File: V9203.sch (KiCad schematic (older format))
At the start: 36 parts, among them J1 RJ45, J4 Screw_Terminal_1x04, U1 V9203, Y1 Crystal_GND24

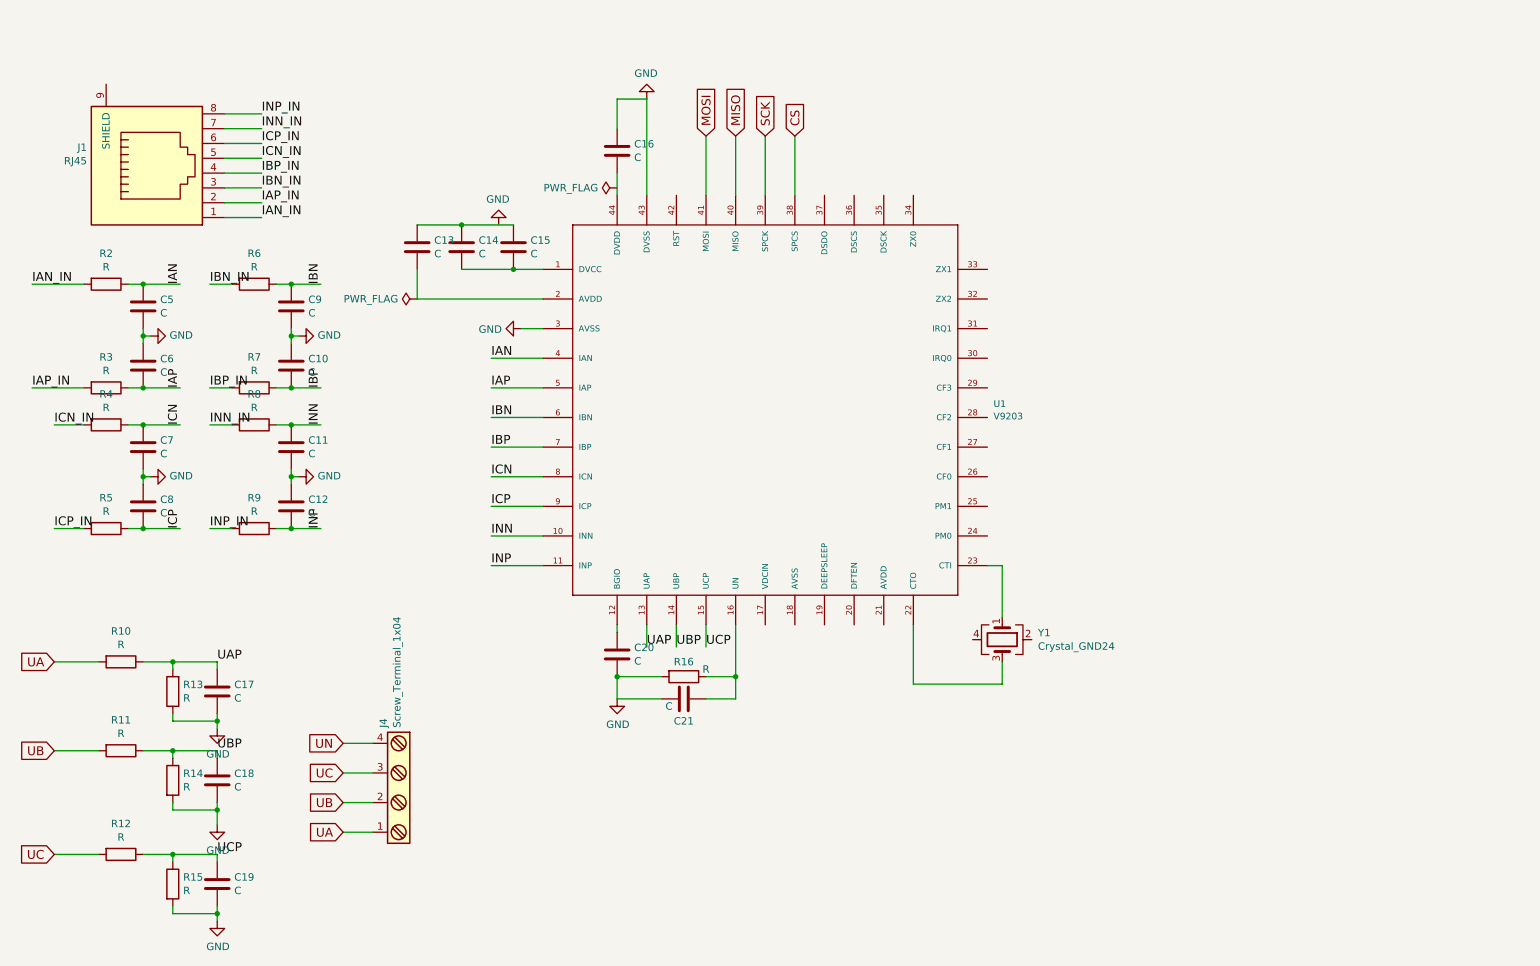
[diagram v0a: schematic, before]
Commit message: Added more parts to featherwing
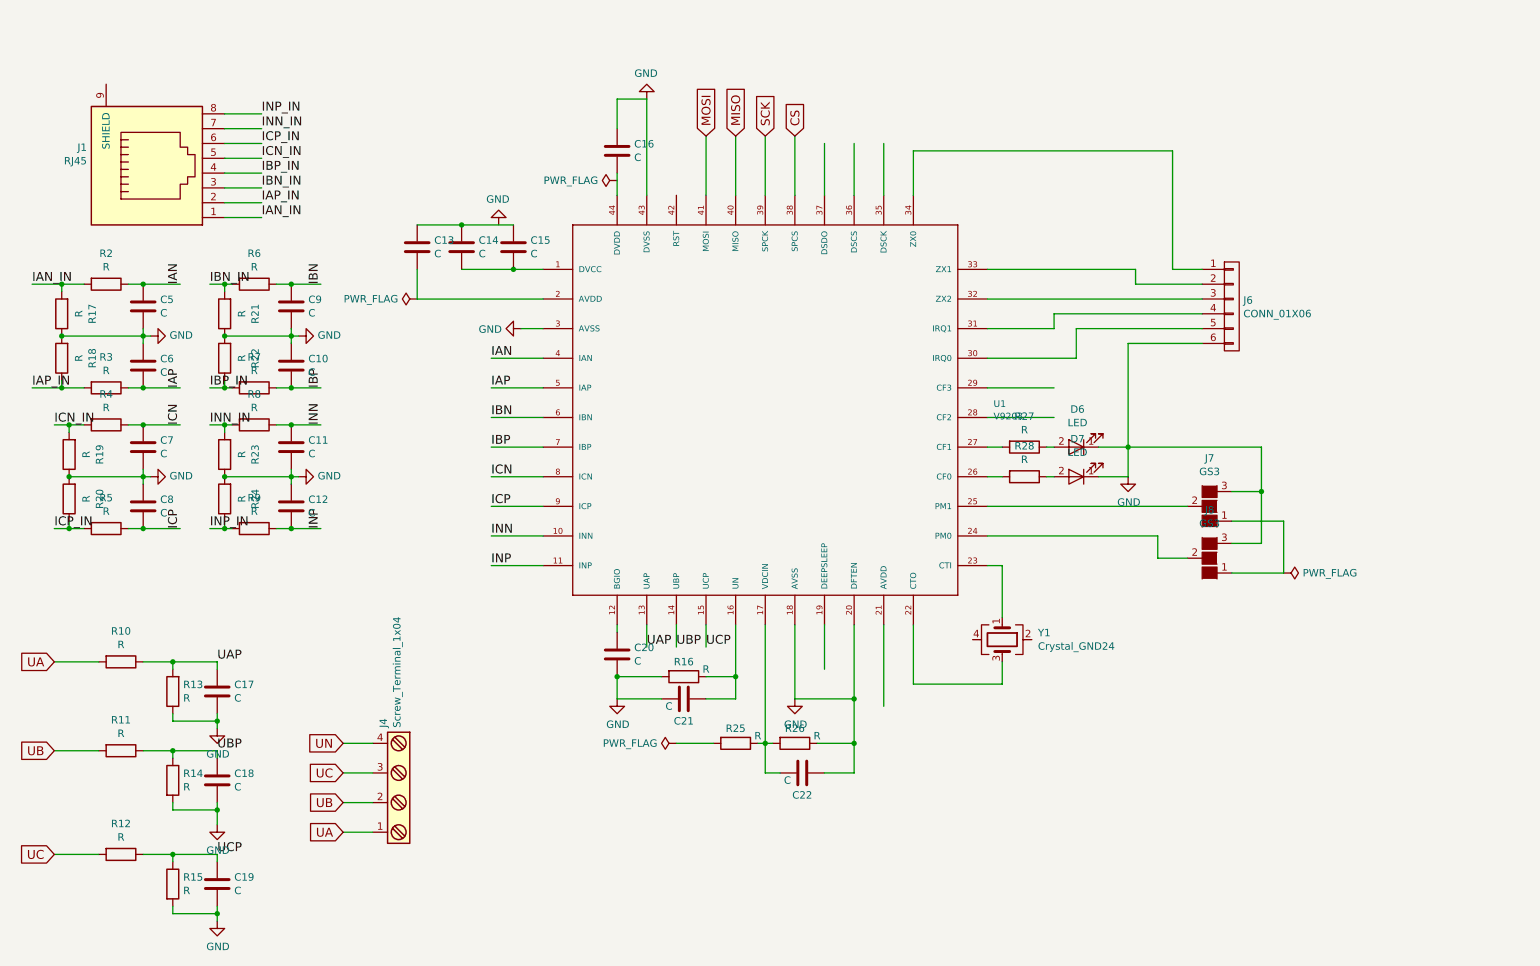
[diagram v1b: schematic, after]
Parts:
- added C22: C, Capacitors_SMD:C_0402, symbol C
- added D6, D7: LED, symbol LED
- added J6: CONN_01X06, symbol CONN_01X06
- added J7, J8: GS3, Connectors:GS3, symbol GS3
- added R17, R18, R19, R20, R21, R22, R23, R24, R25, R26: R, Resistors_SMD:R_0402, symbol R
- added R27, R28: R, symbol R
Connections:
- wire segments 93 -> 149

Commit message: Laid out most parts within PCB bounds
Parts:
- D6, D7: footprint (none) -> LEDs:LED_0603
- J6: footprint (none) -> Connectors_JST:JST_PH_B6B-PH-SM4-TB_06x2.00mm_Straight
- J7, J8: footprint Connectors:GS3 -> Connect:GS3
- R27, R28: footprint (none) -> Resistors_SMD:R_0603_HandSoldering
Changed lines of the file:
@@
 $EndComp
 $Comp
-L GND #PWR11
+L GND #PWR01
 U 1 1 58D7BD25
 P 4900 1350
-F 0 "#PWR11" H 100 -900 50  0001 C CNN
+F 0 "#PWR01" H 100 -900 50  0001 C CNN
 F 1 "GND" H 4905 1177 50  0000 C CNN
 F 2 "" H 100 -650 50  0001 C CNN
@@
 $EndComp
 $Comp
-L PWR_FLAG #FLG2
+L PWR_FLAG #FLG02
 U 1 1 58D7C0C0
 P 4700 1900
-F 0 "#FLG2" H -150 75  50  0001 C CNN
+F 0 "#FLG02" H -150 75  50  0001 C CNN
 F 1 "PWR_FLAG" V 4700 2028 50  0000 L CNN
 F 2 "" H -150 0   50  0001 C CNN
@@
 $EndComp
 $Comp
-L GND #PWR9
+L GND #PWR03
 U 1 1 58D7CCEA
 P 4050 2900
-F 0 "#PWR9" H -750 650 50  0001 C CNN
+F 0 "#PWR03" H -750 650 50  0001 C CNN
 F 1 "GND" V 4055 2772 50  0000 R CNN
 F 2 "" H -750 900 50  0001 C CNN
@@
 $EndComp
 $Comp
-L GND #PWR8
+L GND #PWR04
 U 1 1 58D7CDA6
 P 3900 2200
-F 0 "#PWR8" H -900 -50 50  0001 C CNN
+F 0 "#PWR04" H -900 -50 50  0001 C CNN
 F 1 "GND" H 3905 2027 50  0000 C CNN
 F 2 "" H -900 200 50  0001 C CNN
@@
 $EndComp
 $Comp
-L PWR_FLAG #FLG1
+L PWR_FLAG #FLG05
 U 1 1 58D7CE59
 P 3350 2700
-F 0 "#FLG1" H -1500 875 50  0001 C CNN
+F 0 "#FLG05" H -1500 875 50  0001 C CNN
 F 1 "PWR_FLAG" V 3350 2828 50  0000 L CNN
 F 2 "" H -1500 800 50  0001 C CNN
@@
 $EndComp
 $Comp
-L GND #PWR1
+L GND #PWR06
 U 1 1 58D7E932
 P 1550 2950
-F 0 "#PWR1" H -3250 700 50  0001 C CNN
+F 0 "#PWR06" H -3250 700 50  0001 C CNN
 F 1 "GND" V 1555 2822 50  0000 R CNN
 F 2 "" H -3250 950 50  0001 C CNN
@@
 $EndComp
 $Comp
-L GND #PWR2
+L GND #PWR07
 U 1 1 58D7EE20
 P 1550 3900
-F 0 "#PWR2" H -3250 1650 50  0001 C CNN
+F 0 "#PWR07" H -3250 1650 50  0001 C CNN
 F 1 "GND" V 1555 3772 50  0000 R CNN
 F 2 "" H -3250 1900 50  0001 C CNN
@@
 $EndComp
 $Comp
-L GND #PWR7
+L GND #PWR08
 U 1 1 58D7EE5B
 P 2550 3900
-F 0 "#PWR7" H -2250 1650 50  0001 C CNN
+F 0 "#PWR08" H -2250 1650 50  0001 C CNN
 F 1 "GND" V 2555 3772 50  0000 R CNN
 F 2 "" H -2250 1900 50  0001 C CNN
@@
 $EndComp
 $Comp
-L GND #PWR6
+L GND #PWR09
 U 1 1 58D7EE96
 P 2550 2950
-F 0 "#PWR6" H -2250 700 50  0001 C CNN
+F 0 "#PWR09" H -2250 700 50  0001 C CNN
 F 1 "GND" V 2555 2822 50  0000 R CNN
 F 2 "" H -2250 950 50  0001 C CNN
@@
 $EndComp
 $Comp
-L GND #PWR3
+L GND #PWR010
 U 1 1 58D8C933
 P 2000 5600
-F 0 "#PWR3" H -2800 3350 50  0001 C CNN
+F 0 "#PWR010" H -2800 3350 50  0001 C CNN
 F 1 "GND" H 2005 5427 50  0000 C CNN
 F 2 "" H -2800 3600 50  0001 C CNN
@@
 $EndComp
 $Comp
-L GND #PWR4
+L GND #PWR011
 U 1 1 58D8CC7A
 P 2000 6250
-F 0 "#PWR4" H -2800 4000 50  0001 C CNN
+F 0 "#PWR011" H -2800 4000 50  0001 C CNN
 F 1 "GND" H 2005 6077 50  0000 C CNN
 F 2 "" H -2800 4250 50  0001 C CNN
@@
 $EndComp
 $Comp
-L GND #PWR5
+L GND #PWR012
 U 1 1 58D8CE39
 P 2000 6900
-F 0 "#PWR5" H -2800 4650 50  0001 C CNN
+F 0 "#PWR012" H -2800 4650 50  0001 C CNN
 F 1 "GND" H 2005 6727 50  0000 C CNN
 F 2 "" H -2800 4900 50  0001 C CNN
@@
 $EndComp
 $Comp
-L GND #PWR10
+L GND #PWR013
 U 1 1 58D8D54A
 P 4700 5400
-F 0 "#PWR10" H -100 3150 50  0001 C CNN
+F 0 "#PWR013" H -100 3150 50  0001 C CNN
 F 1 "GND" H 4705 5227 50  0000 C CNN
 F 2 "" H -100 3400 50  0001 C CNN
@@
 F 0 "D7" H 7792 3645 50  0000 C CNN
 F 1 "LED" H 7792 3736 50  0000 C CNN
-F 2 "" H -550 250 50  0001 C CNN
+F 2 "LEDs:LED_0603" H -550 250 50  0001 C CNN
 F 3 "" H -550 250 50  0001 C CNN
 	1    7800 3900
@@
 F 0 "D6" H 7792 3445 50  0000 C CNN
 F 1 "LED" H 7792 3536 50  0000 C CNN
-F 2 "" H -550 50  50  0001 C CNN
+F 2 "LEDs:LED_0603" H -550 50  50  0001 C CNN
 F 3 "" H -550 50  50  0001 C CNN
 	1    7800 3700
@@
 F 0 "R27" V 7243 3700 50  0000 C CNN
 F 1 "R" V 7334 3700 50  0000 C CNN
-F 2 "" V -70 0   50  0001 C CNN
+F 2 "Resistors_SMD:R_0603_HandSoldering" V -70 0   50  0001 C CNN
 F 3 "" H 0   0   50  0001 C CNN
 	1    7450 3700
@@
 F 0 "R28" V 7243 3900 50  0000 C CNN
 F 1 "R" V 7334 3900 50  0000 C CNN
-F 2 "" V -70 200 50  0001 C CNN
+F 2 "Resistors_SMD:R_0603_HandSoldering" V -70 200 50  0001 C CNN
 F 3 "" H 0   200 50  0001 C CNN
 	1    7450 3900
@@
 $EndComp
 $Comp
-L GND #PWR13
+L GND #PWR014
 U 1 1 58EFA437
 P 8150 3900
-F 0 "#PWR13" H 3350 1650 50  0001 C CNN
+F 0 "#PWR014" H 3350 1650 50  0001 C CNN
 F 1 "GND" H 8155 3727 50  0000 C CNN
 F 2 "" H 3350 1900 50  0001 C CNN
@@
 $EndComp
 $Comp
-L GND #PWR12
+L GND #PWR015
 U 1 1 58EFBDC4
 P 5900 5400
-F 0 "#PWR12" H 1100 3150 50  0001 C CNN
+F 0 "#PWR015" H 1100 3150 50  0001 C CNN
 F 1 "GND" H 5905 5227 50  0000 C CNN
 F 2 "" H 1100 3400 50  0001 C CNN
@@
 $EndComp
 $Comp
-L PWR_FLAG #FLG3
+L PWR_FLAG #FLG016
 U 1 1 58EFD209
 P 5100 5700
-F 0 "#FLG3" H 250 3875 50  0001 C CNN
+F 0 "#FLG016" H 250 3875 50  0001 C CNN
 F 1 "PWR_FLAG" V 5100 5828 50  0000 L CNN
 F 2 "" H 250 3800 50  0001 C CNN
@@
 F 0 "J6" H 8928 2791 50  0000 L CNN
 F 1 "CONN_01X06" H 8928 2700 50  0000 L CNN
-F 2 "" H -100 150 50  0001 C CNN
+F 2 "Connectors_JST:JST_PH_B6B-PH-SM4-TB_06x2.00mm_Straight" H -100 150 50  0001 C CNN
 F 3 "" H -100 150 50  0001 C CNN
 	1    8850 2750
@@
 F 0 "J7" H 8700 3775 50  0000 C CNN
 F 1 "GS3" H 8700 3866 50  0000 C CNN
-F 2 "Connectors:GS3" V -762 -1174 50  0001 C CNN
+F 2 "Connect:GS3" V -762 -1174 50  0001 C CNN
 F 3 "" H -850 -1100 50  0001 C CNN
 	1    8700 4100
@@
 F 0 "J8" H 8700 4125 50  0000 C CNN
 F 1 "GS3" H 8700 4216 50  0000 C CNN
-F 2 "Connectors:GS3" V -762 -824 50  0001 C CNN
+F 2 "Connect:GS3" V -762 -824 50  0001 C CNN
 F 3 "" H -850 -750 50  0001 C CNN
 	1    8700 4450
@@
 Connection ~ 9050 4000
 $Comp
-L PWR_FLAG #FLG4
+L PWR_FLAG #FLG017
 U 1 1 58F50052
 P 9200 4550
-F 0 "#FLG4" H 4350 2725 50  0001 C CNN
+F 0 "#FLG017" H 4350 2725 50  0001 C CNN
 F 1 "PWR_FLAG" V 9200 4678 50  0000 L CNN
 F 2 "" H 4350 2650 50  0001 C CNN

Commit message: Neaten up parts layout
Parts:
- added C? (x4): C, Capacitors_SMD:C_0402, symbol C
- added R? (x4): R, Resistors_SMD:R_0402, symbol R
- R17, R18, R19, R20, R21, R22, R23, R24: footprint Resistors_SMD:R_0402 -> Resistors_SMD:R_0603
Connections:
- net labels added: +3V3, V_CLK, V_CS, V_MISO, V_MOSI
- wire segments 149 -> 167
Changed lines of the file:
@@
 Text Label 3850 4500 0    60   ~ 0
 INP
-Text GLabel 5300 1600 1    60   Input ~ 0
-MOSI
-Text GLabel 5500 1600 1    60   Input ~ 0
-MISO
-Text GLabel 5700 1600 1    60   Input ~ 0
-SCK
-Text GLabel 5900 1600 1    60   Input ~ 0
-CS
 $Comp
 L LED D7
@@
 F 0 "R17" V 743 2800 50  0000 C CNN
 F 1 "R" V 834 2800 50  0000 C CNN
-F 2 "Resistors_SMD:R_0402" V -1670 650 50  0001 C CNN
+F 2 "Resistors_SMD:R_0603" V -1670 650 50  0001 C CNN
 F 3 "" H -1600 650 50  0001 C CNN
 	1    950  2800
@@
 F 0 "R18" V 743 3100 50  0000 C CNN
 F 1 "R" V 834 3100 50  0000 C CNN
-F 2 "Resistors_SMD:R_0402" V -1670 950 50  0001 C CNN
+F 2 "Resistors_SMD:R_0603" V -1670 950 50  0001 C CNN
 F 3 "" H -1600 950 50  0001 C CNN
 	1    950  3100
@@
 F 0 "R21" V 1843 2800 50  0000 C CNN
 F 1 "R" V 1934 2800 50  0000 C CNN
-F 2 "Resistors_SMD:R_0402" V -570 650 50  0001 C CNN
+F 2 "Resistors_SMD:R_0603" V -570 650 50  0001 C CNN
 F 3 "" H -500 650 50  0001 C CNN
 	1    2050 2800
@@
 F 0 "R22" V 1843 3100 50  0000 C CNN
 F 1 "R" V 1934 3100 50  0000 C CNN
-F 2 "Resistors_SMD:R_0402" V -570 950 50  0001 C CNN
+F 2 "Resistors_SMD:R_0603" V -570 950 50  0001 C CNN
 F 3 "" H -500 950 50  0001 C CNN
 	1    2050 3100
@@
 F 0 "R19" V 793 3750 50  0000 C CNN
 F 1 "R" V 884 3750 50  0000 C CNN
-F 2 "Resistors_SMD:R_0402" V -1620 1600 50  0001 C CNN
+F 2 "Resistors_SMD:R_0603" V -1620 1600 50  0001 C CNN
 F 3 "" H -1550 1600 50  0001 C CNN
 	1    1000 3750
@@
 F 0 "R20" V 793 4050 50  0000 C CNN
 F 1 "R" V 884 4050 50  0000 C CNN
-F 2 "Resistors_SMD:R_0402" V -1620 1900 50  0001 C CNN
+F 2 "Resistors_SMD:R_0603" V -1620 1900 50  0001 C CNN
 F 3 "" H -1550 1900 50  0001 C CNN
 	1    1000 4050
@@
 F 0 "R23" V 1843 3750 50  0000 C CNN
 F 1 "R" V 1934 3750 50  0000 C CNN
-F 2 "Resistors_SMD:R_0402" V -570 1600 50  0001 C CNN
+F 2 "Resistors_SMD:R_0603" V -570 1600 50  0001 C CNN
 F 3 "" H -500 1600 50  0001 C CNN
 	1    2050 3750
@@
 F 0 "R24" V 1843 4050 50  0000 C CNN
 F 1 "R" V 1934 4050 50  0000 C CNN
-F 2 "Resistors_SMD:R_0402" V -570 1900 50  0001 C CNN
+F 2 "Resistors_SMD:R_0603" V -570 1900 50  0001 C CNN
 F 3 "" H -500 1900 50  0001 C CNN
 	1    2050 4050
@@
 	0    1    1    0
 $EndComp
+Text GLabel 5200 5700 3    60   Input ~ 0
++3V3
+Text GLabel 9100 4550 3    60   Input ~ 0
++3V3
+$Comp
+L R R?
+U 1 1 58FE5B05
+P 10100 2450
+F 0 "R?" V 9893 2450 50  0000 C CNN
+F 1 "R" V 9984 2450 50  0000 C CNN
+F 2 "Resistors_SMD:R_0402" V 7480 300 50  0001 C CNN
+F 3 "" H 7550 300 50  0001 C CNN
+	1    10100 2450
+	0    1    1    0
+$EndComp
+$Comp
+L C C?
+U 1 1 58FE5BE7
+P 10300 2650
+F 0 "C?" H 10415 2696 50  0000 L CNN
+F 1 "C" H 10415 2605 50  0000 L CNN
+F 2 "Capacitors_SMD:C_0402" H 8738 -450 50  0001 C CNN
+F 3 "" H 8700 -300 50  0001 C CNN
+	1    10300 2650
+	1    0    0    -1
+$EndComp
+$Comp
+L R R?
+U 1 1 58FE5CF5
+P 10100 3000
+F 0 "R?" V 9893 3000 50  0000 C CNN
+F 1 "R" V 9984 3000 50  0000 C CNN
+F 2 "Resistors_SMD:R_0402" V 7480 850 50  0001 C CNN
+F 3 "" H 7550 850 50  0001 C CNN
+	1    10100 3000
+	0    1    1    0
+$EndComp
+$Comp
+L C C?
+U 1 1 58FE5D9B
+P 10300 3200
+F 0 "C?" H 10415 3246 50  0000 L CNN
+F 1 "C" H 10415 3155 50  0000 L CNN
+F 2 "Capacitors_SMD:C_0402" H 8738 100 50  0001 C CNN
+F 3 "" H 8700 250 50  0001 C CNN
+	1    10300 3200
+	1    0    0    -1
+$EndComp
+$Comp
+L R R?
+U 1 1 58FE5E43
+P 10050 3500
+F 0 "R?" V 9843 3500 50  0000 C CNN
+F 1 "R" V 9934 3500 50  0000 C CNN
+F 2 "Resistors_SMD:R_0402" V 7430 1350 50  0001 C CNN
+F 3 "" H 7500 1350 50  0001 C CNN
+	1    10050 3500
+	0    1    1    0
+$EndComp
+$Comp
+L C C?
+U 1 1 58FE5EEF
+P 10300 3700
+F 0 "C?" H 10415 3746 50  0000 L CNN
+F 1 "C" H 10415 3655 50  0000 L CNN
+F 2 "Capacitors_SMD:C_0402" H 8738 600 50  0001 C CNN
+F 3 "" H 8700 750 50  0001 C CNN
+	1    10300 3700
+	1    0    0    -1
+$EndComp
+$Comp
+L C C?
+U 1 1 58FE5F95
+P 9850 4250
+F 0 "C?" H 9965 4296 50  0000 L CNN
+F 1 "C" H 9965 4205 50  0000 L CNN
+F 2 "Capacitors_SMD:C_0402" H 8288 1150 50  0001 C CNN
+F 3 "" H 8250 1300 50  0001 C CNN
+	1    9850 4250
+	1    0    0    -1
+$EndComp
+$Comp
+L R R?
+U 1 1 58FE6045
+P 10050 4000
+F 0 "R?" V 9843 4000 50  0000 C CNN
+F 1 "R" V 9934 4000 50  0000 C CNN
+F 2 "Resistors_SMD:R_0402" V 7430 1850 50  0001 C CNN
+F 3 "" H 7500 1850 50  0001 C CNN
+	1    10050 4000
+	0    1    1    0
+$EndComp
+Text Label 5300 1600 1    60   ~ 0
+V_MOSI
+Text Label 5500 1600 1    60   ~ 0
+V_MISO
+Text Label 5700 1600 1    60   ~ 0
+V_CLK
+Text Label 5900 1600 1    60   ~ 0
+V_CS
+Wire Wire Line
+	10250 2450 10450 2450
+Wire Wire Line
+	10300 2450 10300 2500
+Connection ~ 10300 2450
+Wire Wire Line
+	10250 3000 10450 3000
+Wire Wire Line
+	10300 3000 10300 3050
+Connection ~ 10300 3000
+Wire Wire Line
+	10200 3500 10450 3500
+Wire Wire Line
+	10300 3500 10300 3550
+Connection ~ 10300 3500
+Wire Wire Line
+	9850 4100 9850 4000
+Connection ~ 9850 4000
+Wire Wire Line
+	10200 4000 10400 4000
+$Comp
+L GND #PWR?
+U 1 1 58FE85DB
+P 10600 4500
+F 0 "#PWR?" H 5800 2250 50  0001 C CNN
+F 1 "GND" H 10605 4327 50  0000 C CNN
+F 2 "" H 5800 2500 50  0001 C CNN
+F 3 "" H 5800 2500 50  0001 C CNN
+	1    10600 4500
+	1    0    0    -1
+$EndComp
+Wire Wire Line
+	9850 4400 9850 4500
+Wire Wire Line
+	9850 4500 10600 4500
+Wire Wire Line
+	10300 3850 10600 3850
+Wire Wire Line
+	10600 4500 10600 2800
+Wire Wire Line
+	10600 3350 10300 3350
+Connection ~ 10600 3850
+Wire Wire Line
+	10600 2800 10300 2800
+Connection ~ 10600 3350
+Wire Wire Line
+	9950 2450 9750 2450
+Wire Wire Line
+	9950 3000 9750 3000
+Wire Wire Line
+	9900 3500 9750 3500
+Wire Wire Line
+	9900 4000 9750 4000
+Text Label 10450 2450 0    60   ~ 0
+V_CS
+Text Label 10450 3000 0    60   ~ 0
+V_CLK
+Text Label 10450 3500 0    60   ~ 0
+V_MOSI
+Text Label 10400 4000 0    60   ~ 0
+V_MISO
+Text GLabel 9750 2450 0    60   Input ~ 0
+CS
+Text GLabel 9750 3000 0    60   Input ~ 0
+SCK
+Text GLabel 9750 3500 0    60   Input ~ 0
+MOSI
+Text GLabel 9750 4000 0    60   Input ~ 0
+MISO
 $EndSCHEMATC

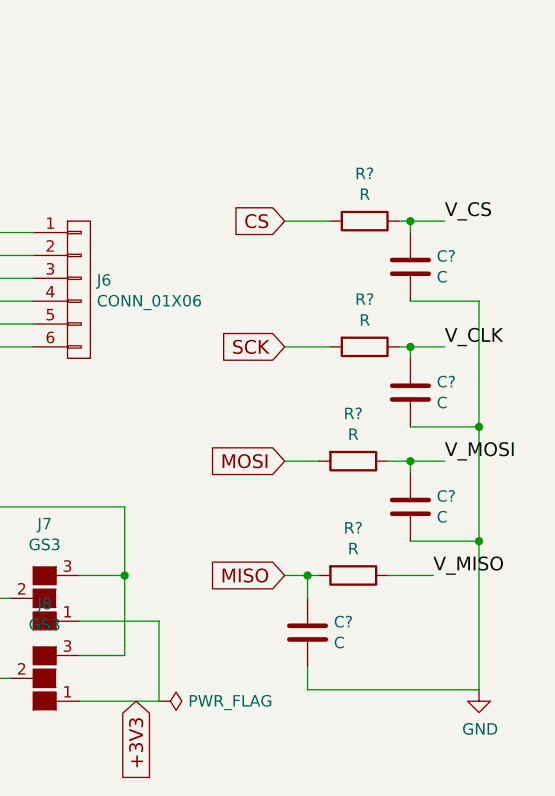
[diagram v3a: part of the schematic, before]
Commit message: Added JST footprints, mounting holes and logos
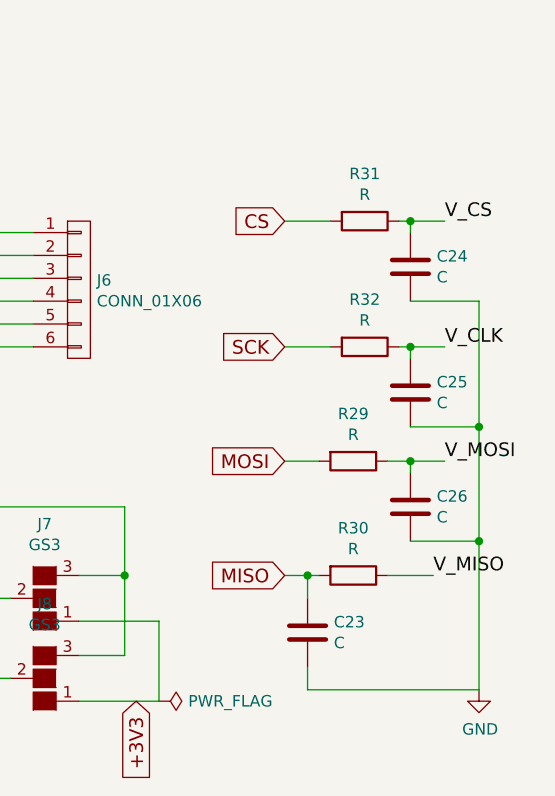
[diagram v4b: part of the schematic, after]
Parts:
- gave numbers to parts that had none: 8
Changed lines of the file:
@@
 LIBS:ROF-78E
 LIBS:GROVE-CONNECTOR-SMD
+LIBS:logo
+LIBS:mechanical
 LIBS:V9203_Devkit-cache
 EELAYER 26 0
@@
 +3V3
 $Comp
-L R R?
+L R R31
 U 1 1 58FE5B05
 P 10100 2450
-F 0 "R?" V 9893 2450 50  0000 C CNN
+F 0 "R31" V 9893 2450 50  0000 C CNN
 F 1 "R" V 9984 2450 50  0000 C CNN
 F 2 "Resistors_SMD:R_0402" V 7480 300 50  0001 C CNN
@@
 $EndComp
 $Comp
-L C C?
+L C C24
 U 1 1 58FE5BE7
 P 10300 2650
-F 0 "C?" H 10415 2696 50  0000 L CNN
+F 0 "C24" H 10415 2696 50  0000 L CNN
 F 1 "C" H 10415 2605 50  0000 L CNN
 F 2 "Capacitors_SMD:C_0402" H 8738 -450 50  0001 C CNN
@@
 $EndComp
 $Comp
-L R R?
+L R R32
 U 1 1 58FE5CF5
 P 10100 3000
-F 0 "R?" V 9893 3000 50  0000 C CNN
+F 0 "R32" V 9893 3000 50  0000 C CNN
 F 1 "R" V 9984 3000 50  0000 C CNN
 F 2 "Resistors_SMD:R_0402" V 7480 850 50  0001 C CNN
@@
 $EndComp
 $Comp
-L C C?
+L C C25
 U 1 1 58FE5D9B
 P 10300 3200
-F 0 "C?" H 10415 3246 50  0000 L CNN
+F 0 "C25" H 10415 3246 50  0000 L CNN
 F 1 "C" H 10415 3155 50  0000 L CNN
 F 2 "Capacitors_SMD:C_0402" H 8738 100 50  0001 C CNN
@@
 $EndComp
 $Comp
-L R R?
+L R R29
 U 1 1 58FE5E43
 P 10050 3500
-F 0 "R?" V 9843 3500 50  0000 C CNN
+F 0 "R29" V 9843 3500 50  0000 C CNN
 F 1 "R" V 9934 3500 50  0000 C CNN
 F 2 "Resistors_SMD:R_0402" V 7430 1350 50  0001 C CNN
@@
 $EndComp
 $Comp
-L C C?
+L C C26
 U 1 1 58FE5EEF
 P 10300 3700
-F 0 "C?" H 10415 3746 50  0000 L CNN
+F 0 "C26" H 10415 3746 50  0000 L CNN
 F 1 "C" H 10415 3655 50  0000 L CNN
 F 2 "Capacitors_SMD:C_0402" H 8738 600 50  0001 C CNN
@@
 $EndComp
 $Comp
-L C C?
+L C C23
 U 1 1 58FE5F95
 P 9850 4250
-F 0 "C?" H 9965 4296 50  0000 L CNN
+F 0 "C23" H 9965 4296 50  0000 L CNN
 F 1 "C" H 9965 4205 50  0000 L CNN
 F 2 "Capacitors_SMD:C_0402" H 8288 1150 50  0001 C CNN
@@
 $EndComp
 $Comp
-L R R?
+L R R30
 U 1 1 58FE6045
 P 10050 4000
-F 0 "R?" V 9843 4000 50  0000 C CNN
+F 0 "R30" V 9843 4000 50  0000 C CNN
 F 1 "R" V 9934 4000 50  0000 C CNN
 F 2 "Resistors_SMD:R_0402" V 7430 1850 50  0001 C CNN
@@
 	10200 4000 10400 4000
 $Comp
-L GND #PWR?
+L GND #PWR018
 U 1 1 58FE85DB
 P 10600 4500
-F 0 "#PWR?" H 5800 2250 50  0001 C CNN
+F 0 "#PWR018" H 5800 2250 50  0001 C CNN
 F 1 "GND" H 10605 4327 50  0000 C CNN
 F 2 "" H 5800 2500 50  0001 C CNN
